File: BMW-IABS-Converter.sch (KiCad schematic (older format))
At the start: 69 parts, among them J1 SWD, J2 HCCPHPE24BKA90F, J3 GPIO_A0, J4 GPIO_A1, J5 GPIO_F0, J6 GPIO_F1, J7 GPIO_A2, J8 GND, Q1 IRFR9024, Q2 IRLML0060TRPbF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

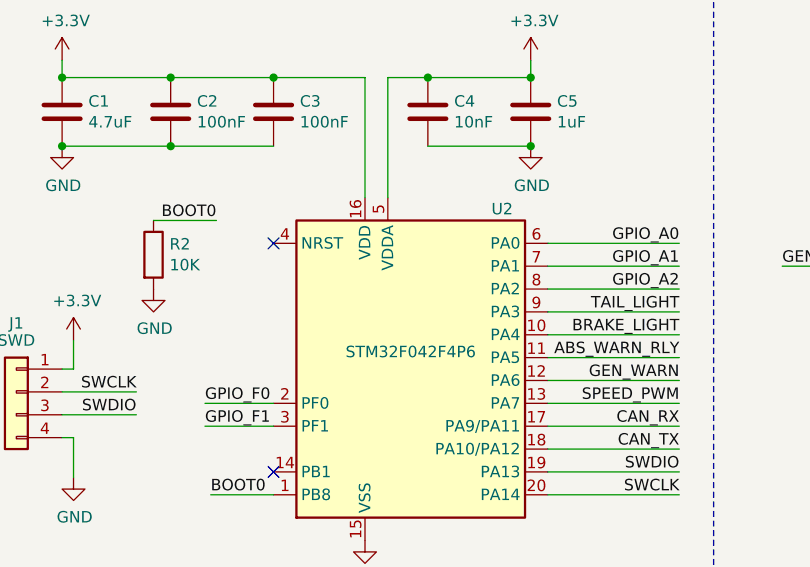
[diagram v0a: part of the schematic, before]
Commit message: Fixed mcu package.
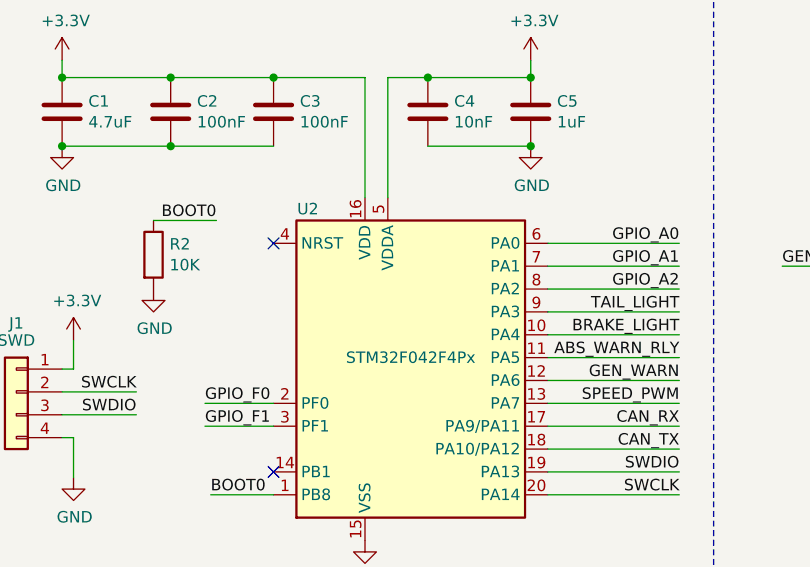
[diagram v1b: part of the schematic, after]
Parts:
- U2: value STM32F042F4P6 -> STM32F042F4Px; footprint Package_SO:SO-20_12.8x7.5mm_P1.27mm -> Package_SO:TSSOP-20_4.4x6.5mm_P0.65mm
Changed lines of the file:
@@
 SWDIO
-$Comp
-L MCU_ST_STM32F0:STM32F042F4Px U?
-U 1 1 60302FF9
-P 2475 2075
-AR Path="/602C3F48/60302FF9" Ref="U?"  Part="1"
-AR Path="/60302FF9" Ref="U2"  Part="1"
-F 0 "U2" H 2875 2725 50  0000 C CNN
-F 1 "STM32F042F4P6" H 2475 2100 50  0000 C CNN
-F 2 "Package_SO:SO-20_12.8x7.5mm_P1.27mm" H 1975 1375 50  0001 R CNN
-F 3 "http://www.ti.com/lit/ds/symlink/lm2904-n.pdf" H 2475 2075 50  0001 C CNN
-	1    2475 2075
-	1    0    0    -1
-$EndComp
 $Comp
 L Regulator_Switching:MC34063AD U6
@@
 Wire Wire Line
 	1000 2425 1000 2600
+$Comp
+L MCU_ST_STM32F0:STM32F042F4Px U2
+U 1 1 60DB6135
+P 2475 2075
+F 0 "U2" H 2025 2725 50  0000 C CNN
+F 1 "STM32F042F4Px" H 2475 2075 50  0000 C CNN
+F 2 "Package_SO:TSSOP-20_4.4x6.5mm_P0.65mm" H 1975 1375 50  0001 R CNN
+F 3 "http://www.st.com/st-web-ui/static/active/en/resource/technical/document/datasheet/DM00105814.pdf" H 2475 2075 50  0001 C CNN
+	1    2475 2075
+	1    0    0    -1
+$EndComp
 $EndSCHEMATC
